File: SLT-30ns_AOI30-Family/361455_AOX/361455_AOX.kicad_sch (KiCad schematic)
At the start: 11 parts, among them U1 12-Pin_SLx_Can

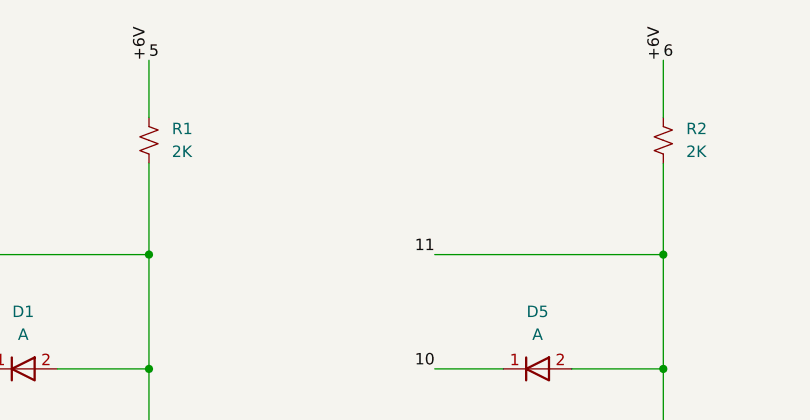
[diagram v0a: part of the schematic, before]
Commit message: Update schematic pdfs
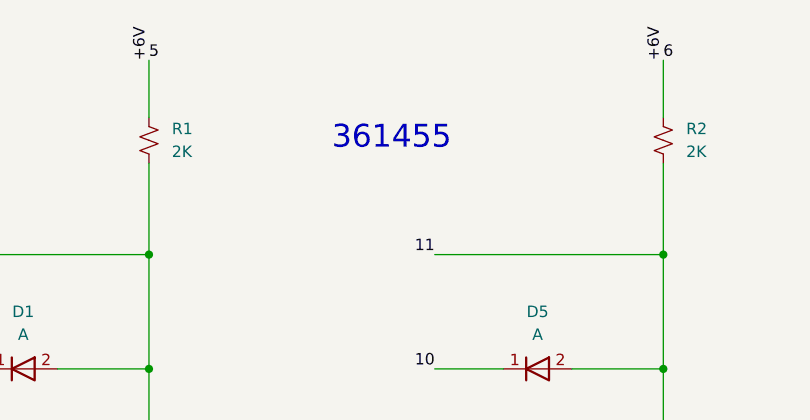
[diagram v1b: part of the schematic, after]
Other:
- note added: "361455"
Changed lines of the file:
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@@
     (effects (font (size 1.27 1.27)) (justify left bottom))
+  )
+  (text "361455" (at 119.38 54.61 0)
+    (effects (font (size 2.54 2.54)) (justify left bottom))
   )
   (label "8" (at 130.81 106.68 180)
